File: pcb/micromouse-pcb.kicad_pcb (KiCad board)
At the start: 2 copper layers, 140 x 100 mm, 40 parts, among them J1_MotorEncoder1 Conn_01x06, J2_MotorEncoder1 Conn_01x06, J3 Conn_01x08, J4 Conn_01x08, Q1 BS170, Q2 TEFT4300, Q3 BS170, Q4 TEFT4300, Q5 BS170, Q6 TEFT4300, Q7 BS170, Q8 TEFT4300, SW1 SW_SPDT, U0 Teensy 4.1, U2 L7805

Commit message: edited pcb
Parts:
- U2: footprint Package_TO_SOT_SMD:TO-252-3_TabPin2 -> Package_TO_SOT_THT:TO-220-3_Vertical
- moved Q3 61.6 mm to (183.5, 67.7)
- moved Q5 61.6 mm to (183.5, 73.5)
- moved Q7 61.6 mm to (183.5, 79.3)
- moved D4 50.3 mm to (155.0, 63.2), turned to -90 degrees
- moved D2 42.5 mm to (153.5, 41.5), turned to -90 degrees
- moved R11 36.4 mm to (118.5, 29.8)
- moved R15 36.4 mm to (124.5, 23.2)
- moved R17 36.4 mm to (124.5, 29.8)
- moved R8 36.4 mm to (118.5, 19.9)
- moved R9 36.4 mm to (118.5, 23.2)
- moved R10 36.4 mm to (118.5, 26.5)
- moved R12 36.4 mm to (118.5, 33.1)
- moved R13 36.4 mm to (118.5, 36.4)
- moved R16 36.4 mm to (124.5, 26.5)
- moved R2 36.4 mm to (112.5, 19.9)
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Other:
- board size 140 x 100 mm -> 90 x 70 mm

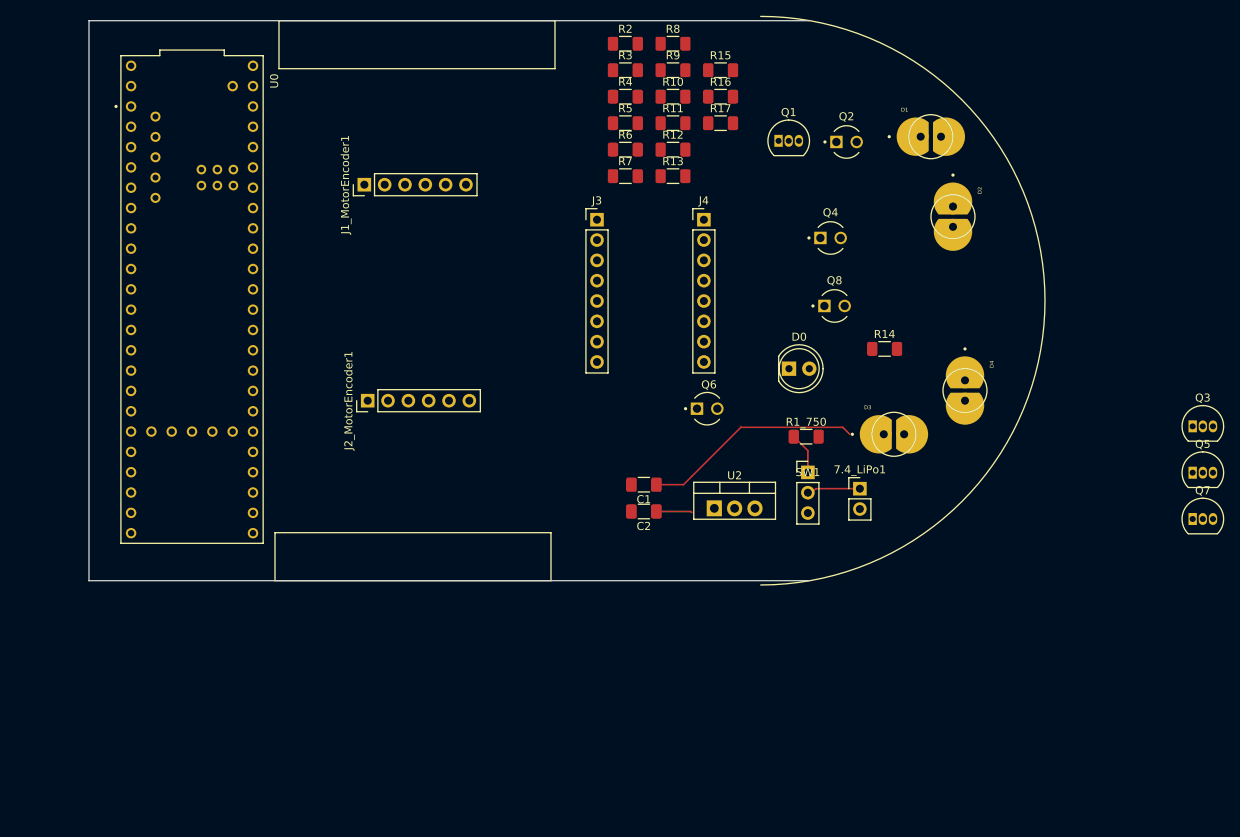
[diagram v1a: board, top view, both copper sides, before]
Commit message: worked on IR placement
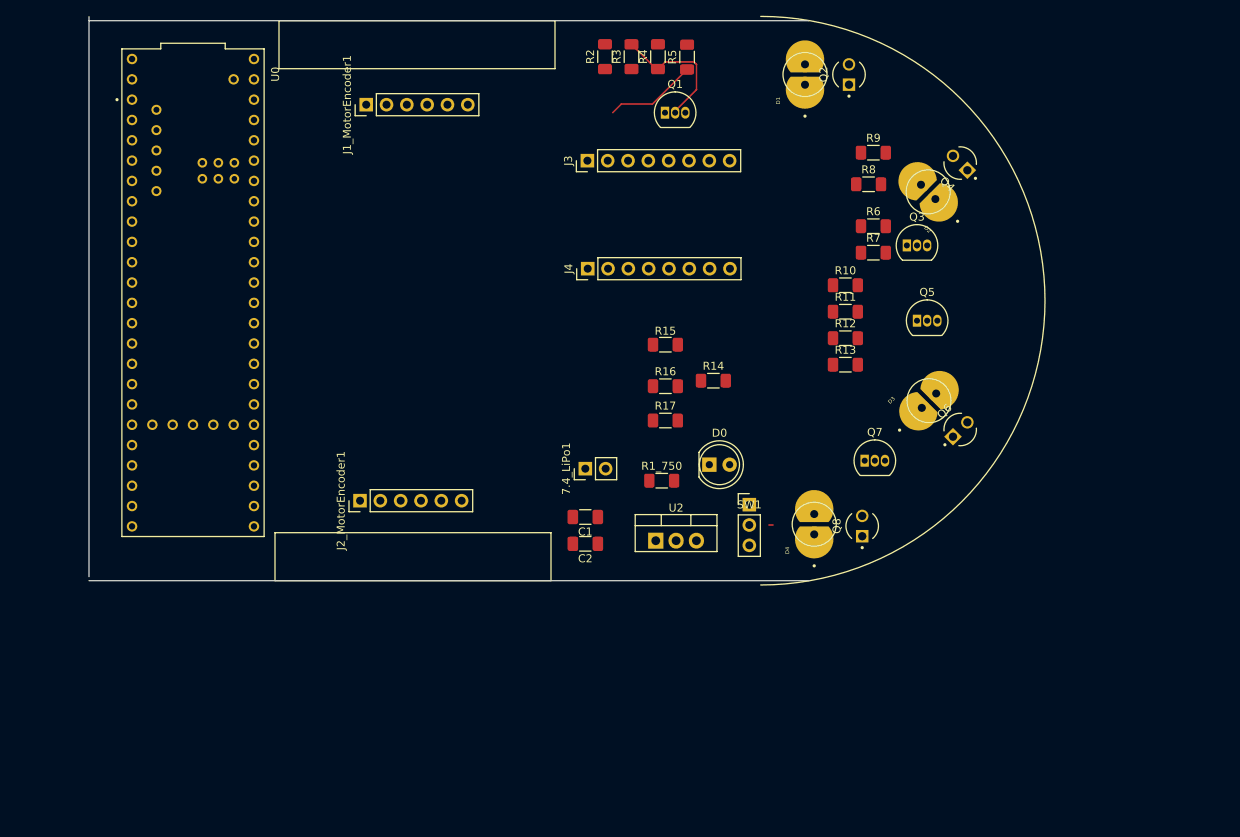
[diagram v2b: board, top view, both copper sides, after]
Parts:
- moved Q3 42.3 mm to (147.7, 45.1)
- moved Q7 41.6 mm to (142.5, 72.0)
- moved Q5 39.4 mm to (149.0, 54.5)
- moved R17 37.8 mm to (117.5, 67.0)
- moved R16 36.8 mm to (117.5, 62.7)
- moved R15 35.0 mm to (117.5, 57.5)
- moved 7.4_LiPo1 34.4 mm to (107.5, 73.0), turned to 90 degrees
- moved R6 32.4 mm to (143.6, 42.7)
- moved R7 32.4 mm to (143.6, 46.0)
- moved R11 31.9 mm to (140.1, 53.4)
- moved R10 31.9 mm to (140.1, 50.1)
- moved R12 31.9 mm to (140.1, 56.7)
- moved R13 31.9 mm to (140.1, 60.0)
- moved Q6 31.7 mm to (154.4, 68.1), turned to 45 degrees
- moved R8 30.1 mm to (142.9, 37.5)
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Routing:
- net 7.4V: track 27.5 -> 0.00 mm
- net Net-(Q1-G): track 0.00 -> 17.1 mm
- net Receiver 1: track 0.00 -> 11.5 mm
- net Net-(7.4_LiPo1-+): track 6.71 -> 0.50 mm
- net Net-(SW1-A): track 5.19 -> 0.00 mm
- net 5V: track 4.50 -> 0.00 mm
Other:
- board size 90 x 70 mm -> 90 x 70.5 mm

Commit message: pcb design not connected yet; awaiting to be roasted in design review
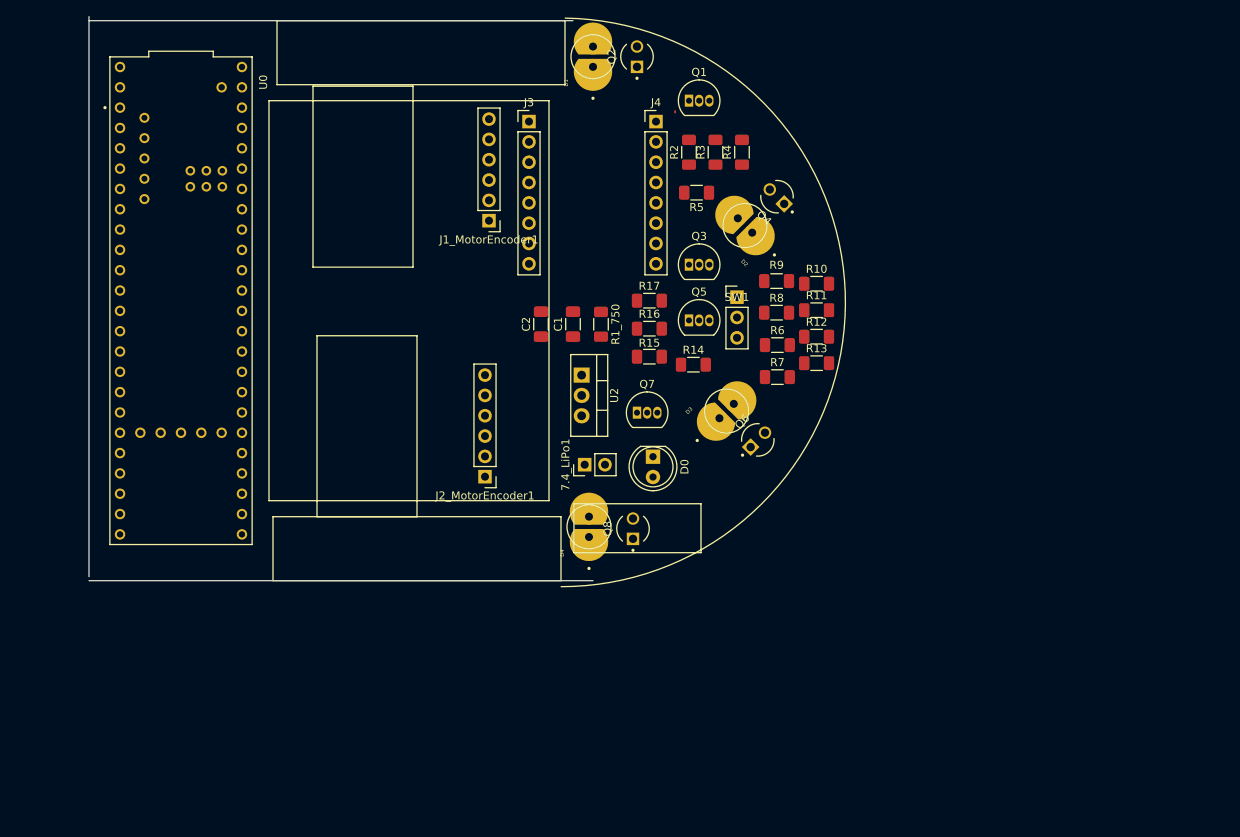
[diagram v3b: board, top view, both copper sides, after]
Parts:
- moved Q7 29.1 mm to (114.0, 66.0)
- moved Q8 28.7 mm to (113.5, 80.5)
- moved Q5 28.5 mm to (120.5, 54.5)
- moved D4 28.2 mm to (108.0, 80.3)
- moved C2 28.0 mm to (102.0, 54.9), turned to 90 degrees
- moved Q3 27.3 mm to (120.5, 47.5)
- moved D1 26.6 mm to (108.5, 21.5)
- moved Q2 26.6 mm to (114.0, 21.5)
- moved SW1 26.0 mm to (126.5, 51.6)
- moved D3 25.3 mm to (125.2, 65.8)
- moved Q6 25.3 mm to (129.1, 69.4)
- moved C1 24.2 mm to (106.0, 54.9), turned to 90 degrees
- moved D2 23.3 mm to (127.5, 42.6)
- moved Q4 23.3 mm to (131.5, 39.0)
- moved U2 22.7 mm to (107.1, 61.3), turned to -90 degrees
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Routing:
- net Net-(Q1-G): track 17.1 -> 0.00 mm
- net Receiver 1: track 11.5 -> 0.00 mm
- net Net-(7.4_LiPo1-+): track 0.50 -> 0.00 mm
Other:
- board size 90 x 70.5 mm -> 63 x 70.5 mm

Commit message: increased width to 8cm, placement done
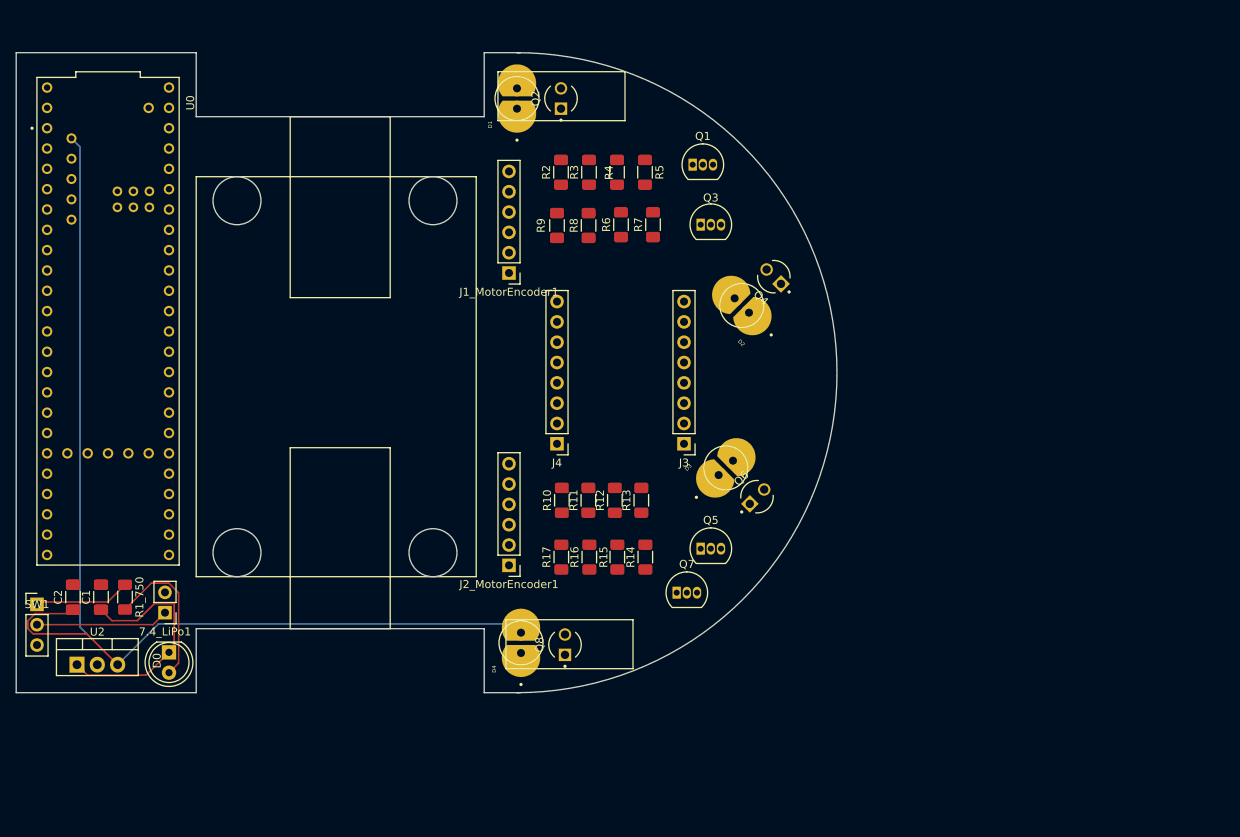
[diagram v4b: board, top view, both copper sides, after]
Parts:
- moved SW1 95.6 mm to (39.0, 90.0)
- moved U2 72.7 mm to (44.0, 97.5), turned to 0 degrees
- moved R1_750 68.6 mm to (50.0, 89.0)
- moved C1 68.2 mm to (47.0, 89.1)
- moved C2 67.7 mm to (43.5, 89.1)
- moved D0 65.3 mm to (55.5, 96.0)
- moved 7.4_LiPo1 55.6 mm to (55.0, 91.0), turned to 180 degrees
- moved J3 44.7 mm to (119.9, 69.9), turned to 180 degrees
- moved J4 42.1 mm to (104.0, 69.9), turned to 180 degrees
- moved R10 41.8 mm to (104.6, 77.0), turned to 90 degrees
- moved R11 37.1 mm to (107.9, 77.0), turned to 90 degrees
- moved R17 33.9 mm to (104.5, 84.0), turned to 90 degrees
- moved R12 32.5 mm to (111.2, 77.0), turned to 90 degrees
- moved R16 29.5 mm to (108.0, 84.0), turned to 90 degrees
- moved Q5 28.6 mm to (122.0, 83.0)
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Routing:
- net 5V: track 0.00 -> 141.5 mm
- net 7.4V: track 0.00 -> 30.2 mm
- net Net-(D0-A): track 0.00 -> 19.0 mm
- net Net-(7.4_LiPo1-+): track 0.00 -> 16.6 mm
- net Net-(SW1-A): track 0.00 -> 12.0 mm
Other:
- board size 63 x 70.5 mm -> 102.6 x 80 mm

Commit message: PCB FINISHED
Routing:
- net 3.3V: track 0.00 -> 264.0 mm, vias 0 -> 4
- net Receiver 3: track 0.00 -> 137.6 mm, vias 0 -> 7
- net Receiver 4: track 0.00 -> 129.4 mm, vias 0 -> 4
- net Receiver 1: track 0.00 -> 119.0 mm, vias 0 -> 3
- net 5V: track 141.5 -> 249.6 mm, vias 0 -> 2
- net Receiver 2: track 0.00 -> 107.7 mm, vias 0 -> 4
- net Emitter 4: track 0.00 -> 104.6 mm, vias 0 -> 2
- net Emitter 2: track 0.00 -> 102.6 mm, vias 0 -> 6
- net GND: track 0.00 -> 96.9 mm, vias 0 -> 2
- net Emitter 3: track 0.00 -> 86.9 mm
- net Emitter 1: track 0.00 -> 73.6 mm, vias 0 -> 4
- net PWM M2_B: track 0.00 -> 62.8 mm
- net PWM M1_B: track 0.00 -> 61.9 mm
- net STBY: track 0.00 -> 61.4 mm
- net PWM M2_A: track 0.00 -> 58.5 mm
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- added copper zone on F.Cu, net GND
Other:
- outline, holes or cut-outs redrawn
